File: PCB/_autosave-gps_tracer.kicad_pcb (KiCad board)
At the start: 2 copper layers, 65 x 38.2 mm, 88 parts, among them IC1 TC4056A, J1 Mic, J2 SPK, J3 I2C, J4 BATTERY, J5 Micro_SD_Card, P1 USB_C_Plug_USB2.0, Q1 S8050, Q2 S8050, Q3 FDN358P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

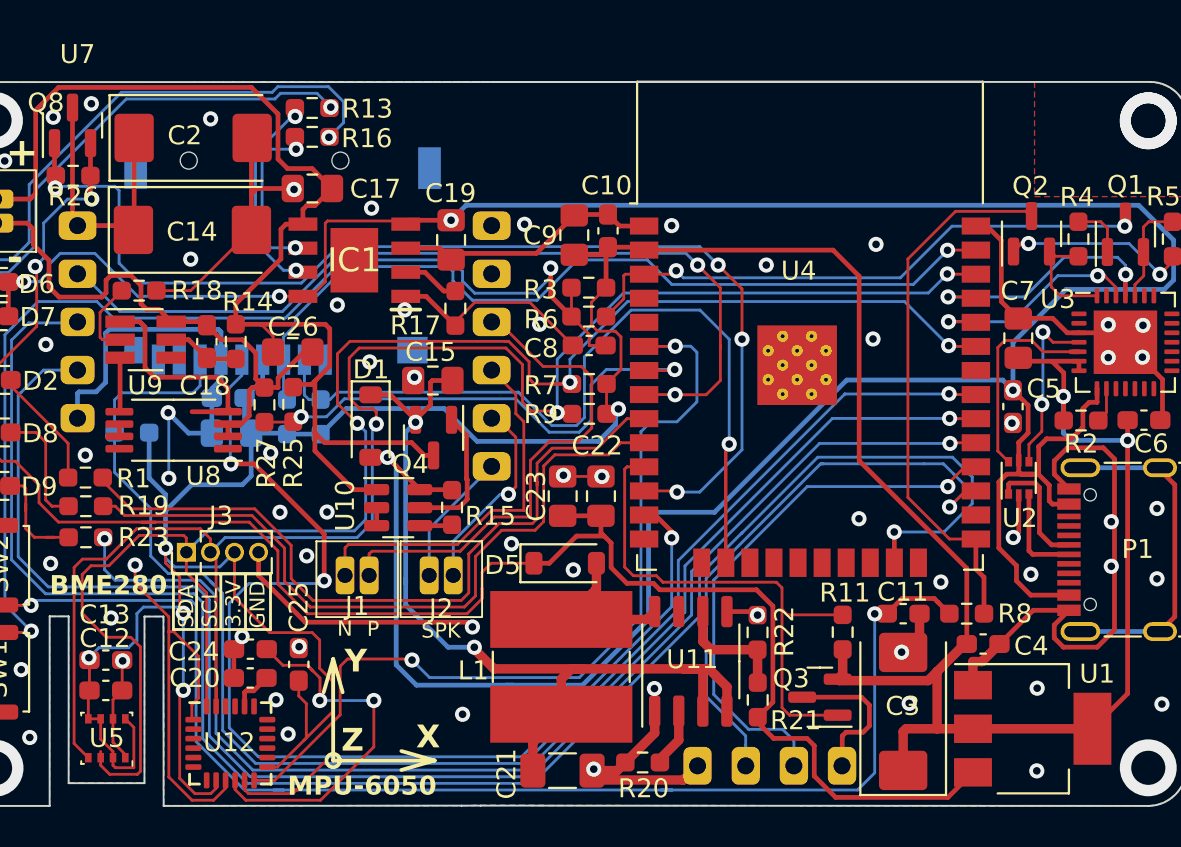
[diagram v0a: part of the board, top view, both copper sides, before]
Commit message: The PCB was traced, and ordered
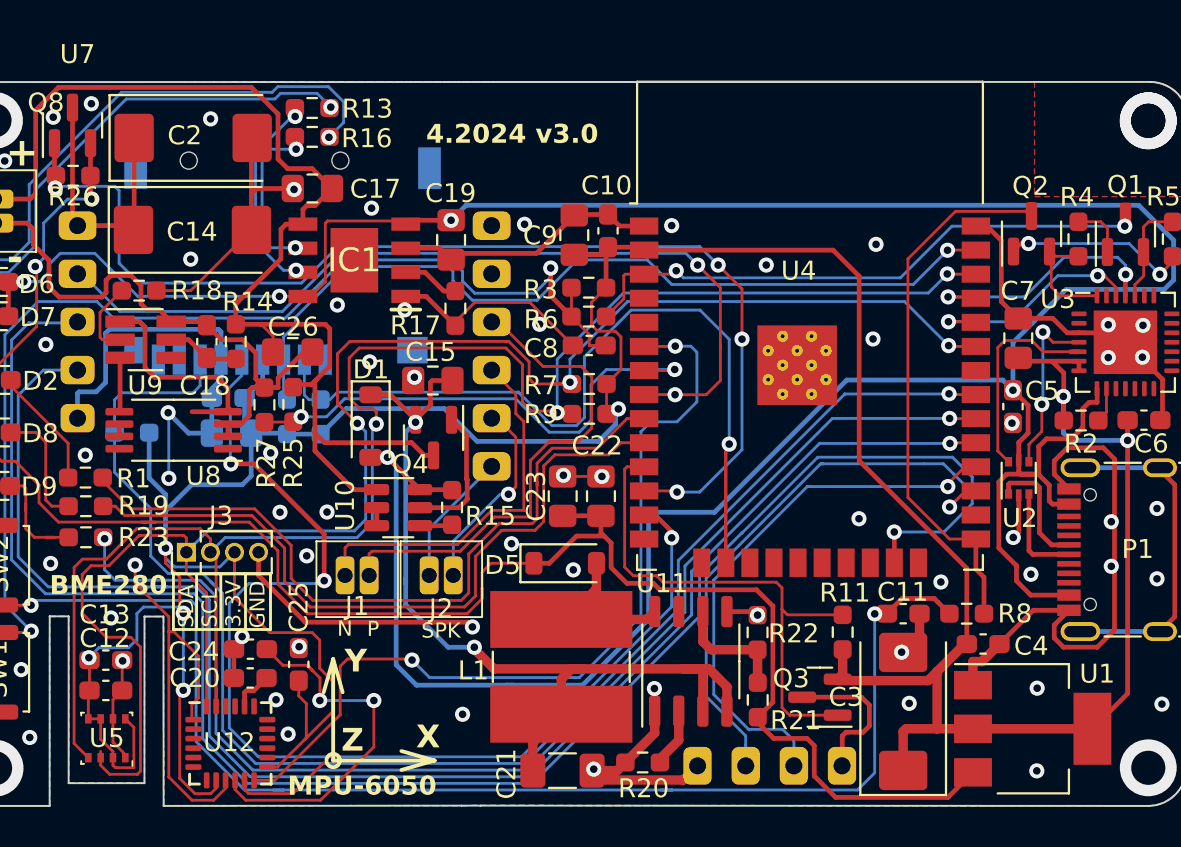
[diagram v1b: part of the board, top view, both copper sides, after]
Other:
- board text added: "4.2024 v3.0"
